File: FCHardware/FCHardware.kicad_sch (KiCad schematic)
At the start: 23 parts, among them J1 XT60Male, J2 Conn_01x02, J3 Conn_01x02, J4 Conn_01x02, J5 Conn_01x02, U1 TPS62125DSG, U2 DRV8833PWP, U3 DRV8833PWP, U5 MPU-6050

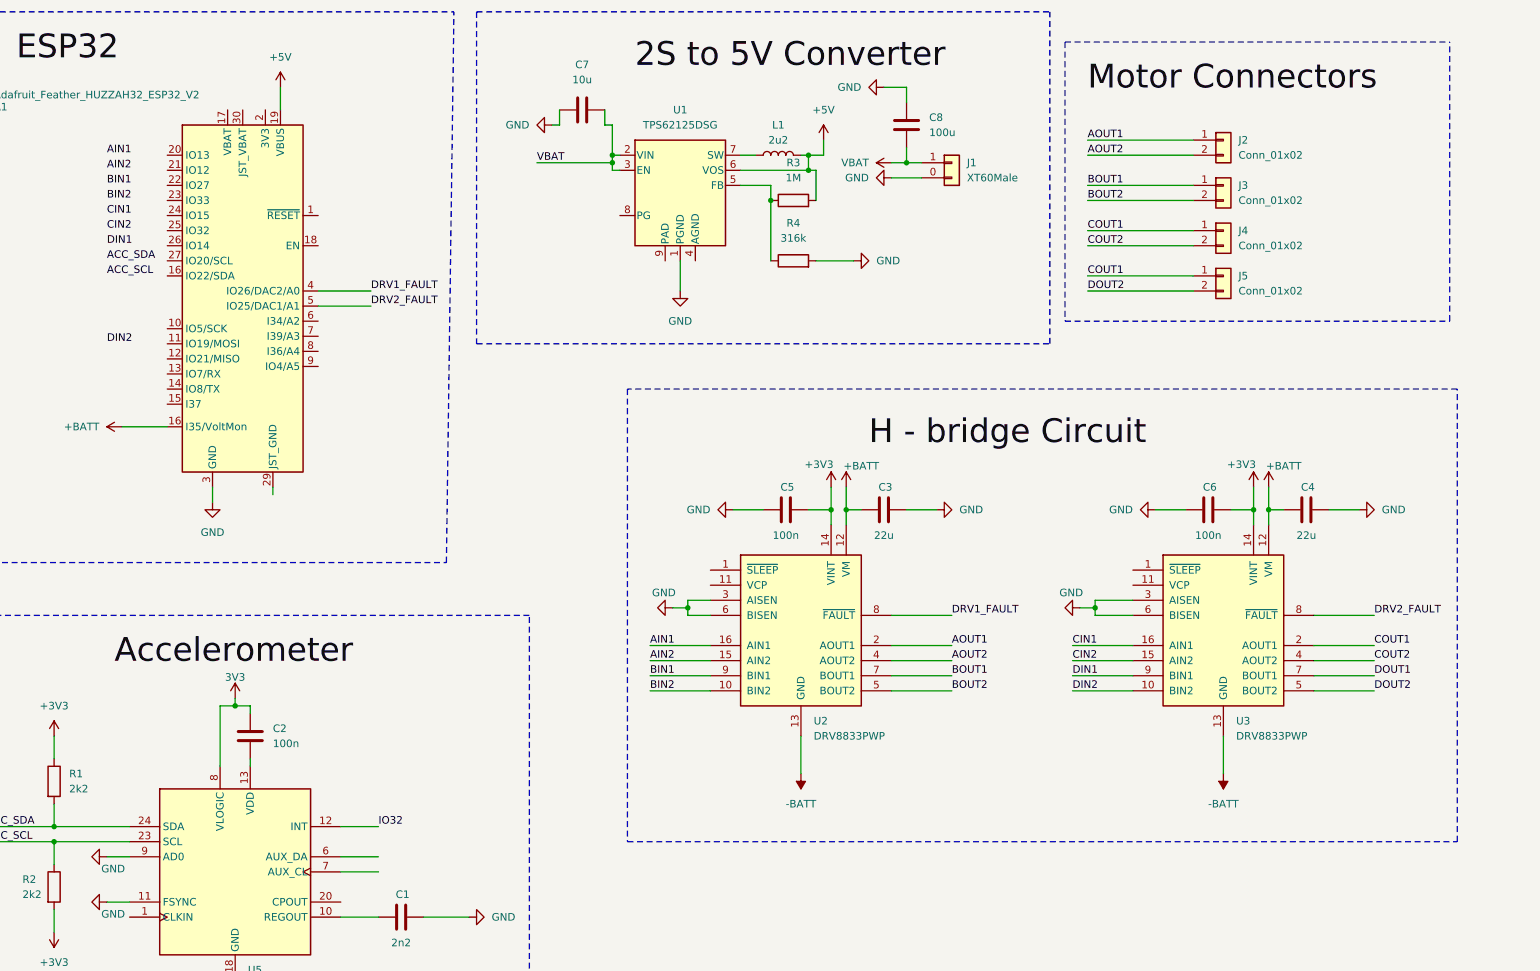
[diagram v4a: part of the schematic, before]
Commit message: Switched from TPS62125 to TPS629203
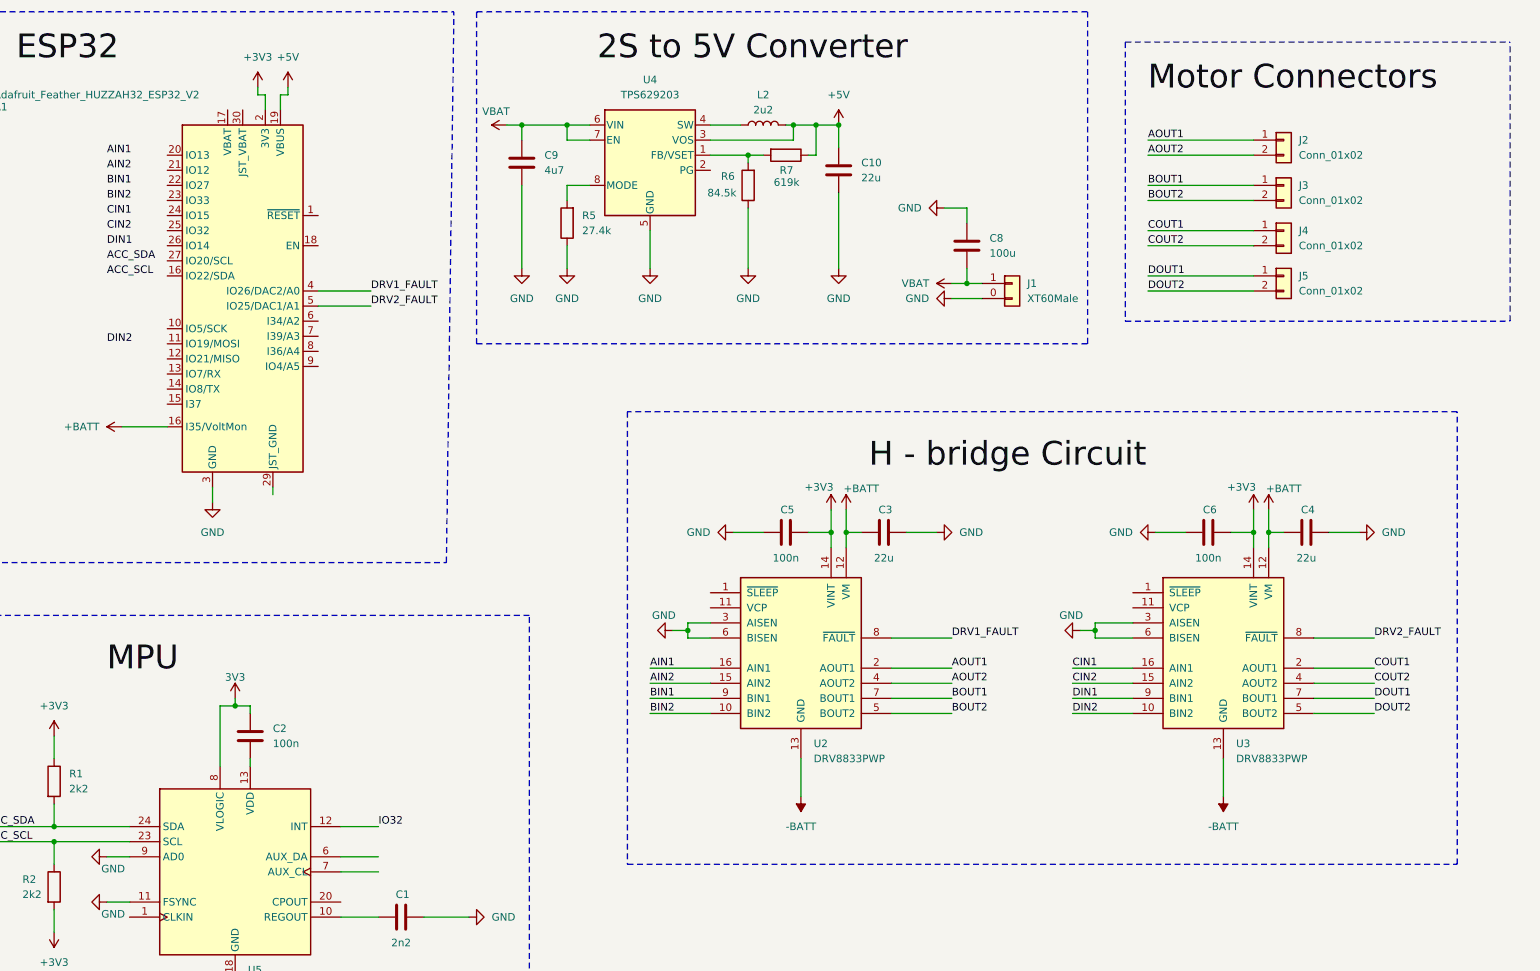
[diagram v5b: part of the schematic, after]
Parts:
- removed C7: 10u, symbol Device:C
- removed L1: 2u2, symbol Device:L
- removed R3: 1M, symbol Device:R
- removed R4: 316k, symbol Device:R
- removed U1: TPS62125DSG, Package_SON:WSON-8-1EP_2x2mm_P0.5mm_EP0.9x1.6mm_ThermalVias, symbol Regulator_Switching:TPS62125DSG
- added C10: 22u, symbol Device:C
- added C9: 4u7, symbol Device:C
- added L2: 2u2, symbol Device:L
- added R5: 27.4k, symbol Device:R
- added R6: 84.5k, symbol Device:R
- added R7: 619k, symbol Device:R
- added U4: TPS629203, Package_SON:WSON-8-1EP_2x2mm_P0.5mm_EP0.9x1.6mm_ThermalVias, symbol CustomSymbols:TPS629203
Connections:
- net +3V3: now also A1.2 (3V3)
- net +5V: now also C10.1, L2.2, R7.1, U4.3 (VOS)
- net COUT1: no longer J5.1 (Pin_1)
- net DOUT1: now also J5.1 (Pin_1)
- net GND: now also C10.2, C9.2, R5.1, R6.1, U4.5 (GND)
- net VBAT: now also C9.1, U4.6 (VIN), U4.7 (EN)
- new net: R6.2, R7.2, U4.1 (FB/VSET)
- new net: L2.1, U4.4 (SW)
- new net: R5.2, U4.8 (MODE)
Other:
- moved on the sheet: C3, C4, C5, C6, C8, J1, J2, J3, J4, J5, U2, U3

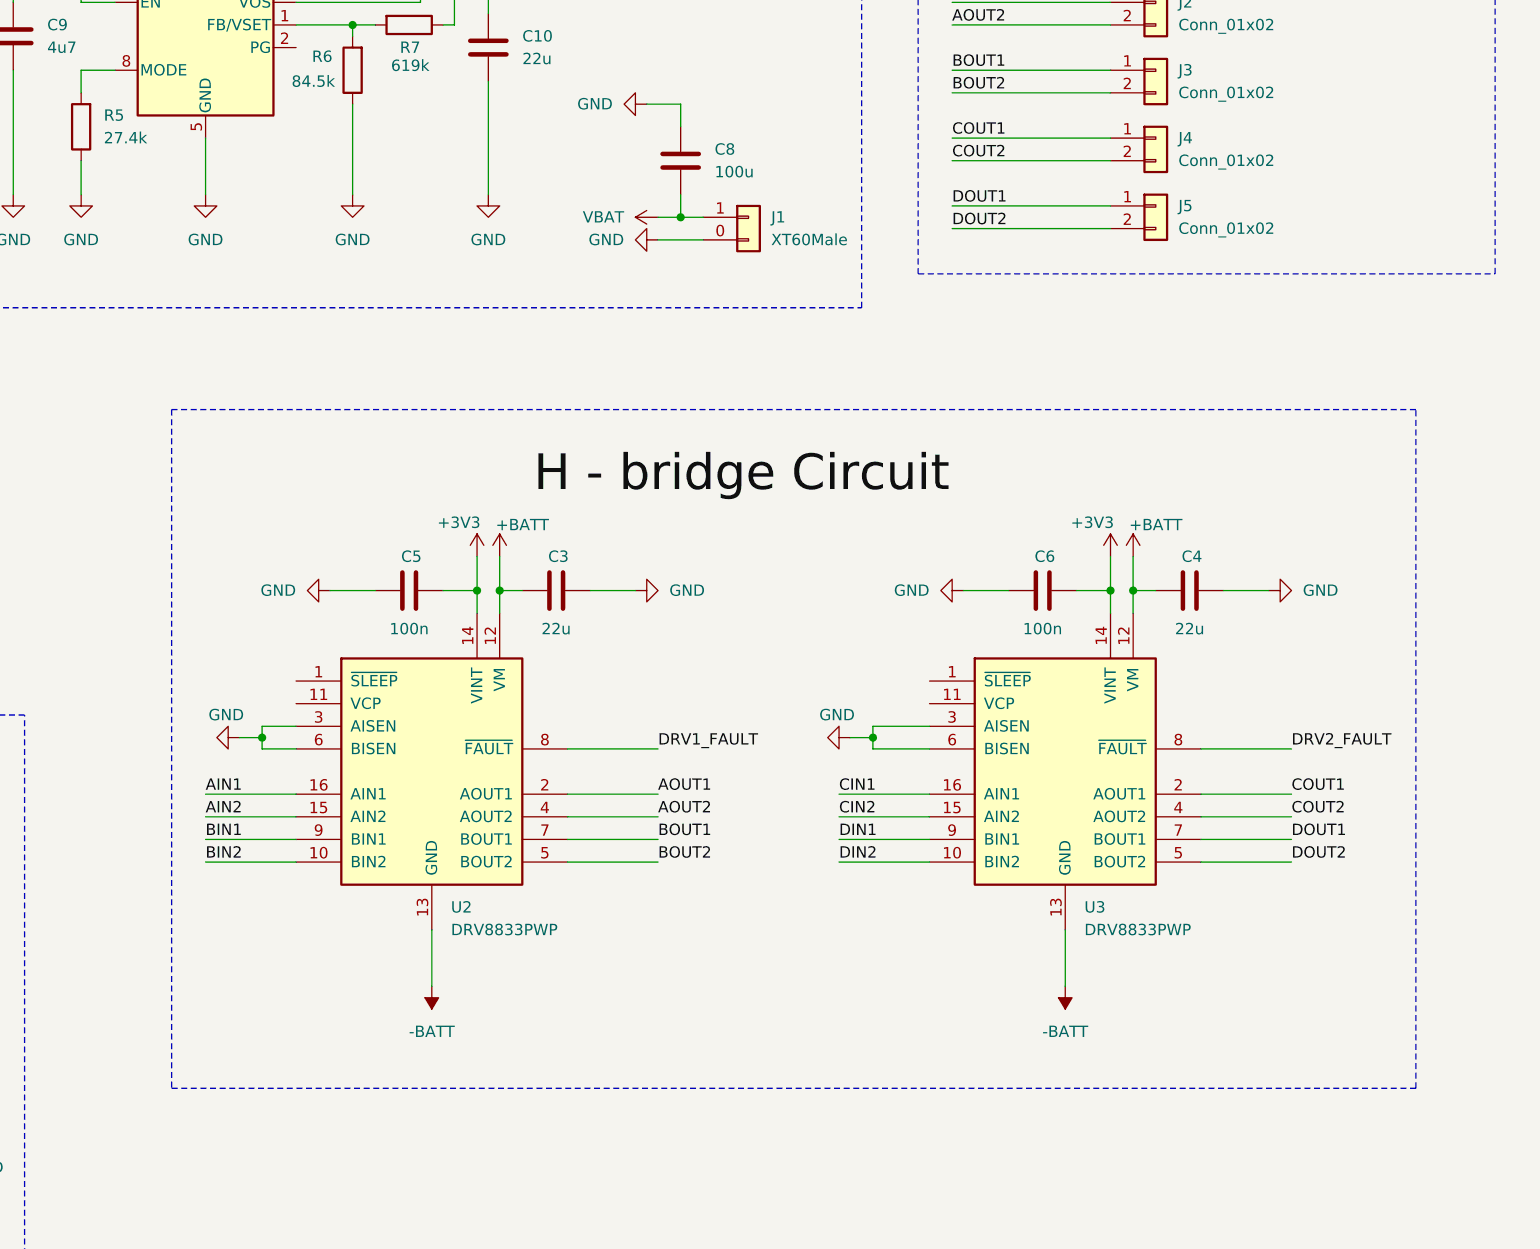
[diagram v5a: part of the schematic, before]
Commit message: Added Xrotor 65A as ESC instead of H-bridges
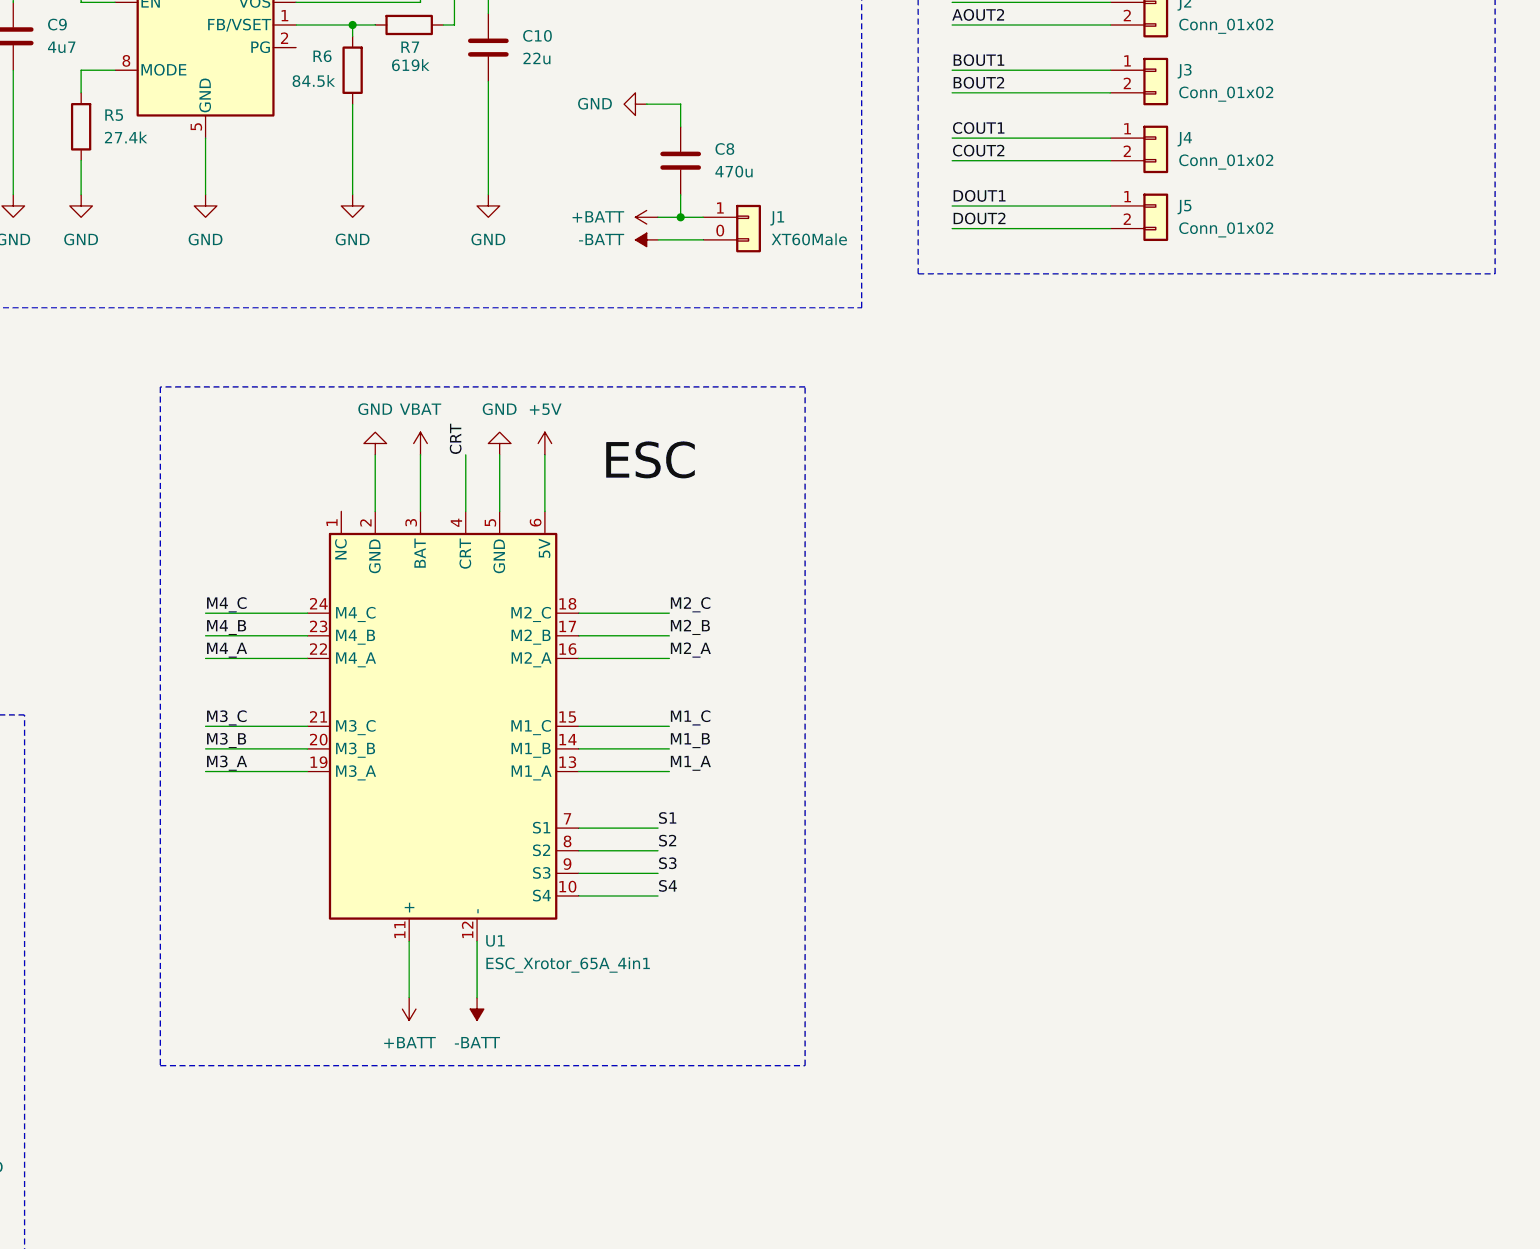
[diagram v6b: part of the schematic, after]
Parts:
- removed C3, C4: 22u, symbol Device:C
- removed C5, C6: 100n, symbol Device:C
- removed U2, U3: DRV8833PWP, Package_SO:HTSSOP-16-1EP_4.4x5mm_P0.65mm_EP3x3mm, symbol Driver_Motor:DRV8833PWP
- added U1: ESC_Xrotor_65A_4in1, -, symbol CustomSymbols:ESC_Xrotor_65A_4in1
- C8: value 100u -> 470u
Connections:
- net +5V: now also U1.6 (5V)
- net +BATT: now also C8.2, J1.1 (+), U1.11 (+)
- net -BATT: now also J1.0 (-), U1.12 (-)
- net GND: now also U1.2 (GND), U1.5 (GND); no longer J1.0 (-)
- net VBAT: now also U1.3 (BAT); no longer C8.2, J1.1 (+)
- new net CRT: U1.4 (CRT)
- new net M1_A: U1.13 (M1_A)
- new net M1_B: U1.14 (M1_B)
- new net M1_C: U1.15 (M1_C)
- new net M2_A: U1.16 (M2_A)
- new net M2_B: U1.17 (M2_B)
- new net M2_C: U1.18 (M2_C)
- new net M3_A: U1.19 (M3_A)
- new net M3_B: U1.20 (M3_B)
- new net M3_C: U1.21 (M3_C)
- new net M4_A: U1.22 (M4_A)
- new net M4_B: U1.23 (M4_B)
- new net M4_C: U1.24 (M4_C)
- new net S1: U1.7 (S1)
- new net S2: U1.8 (S2)
- new net S3: U1.9 (S3)
- new net S4: U1.10 (S4)

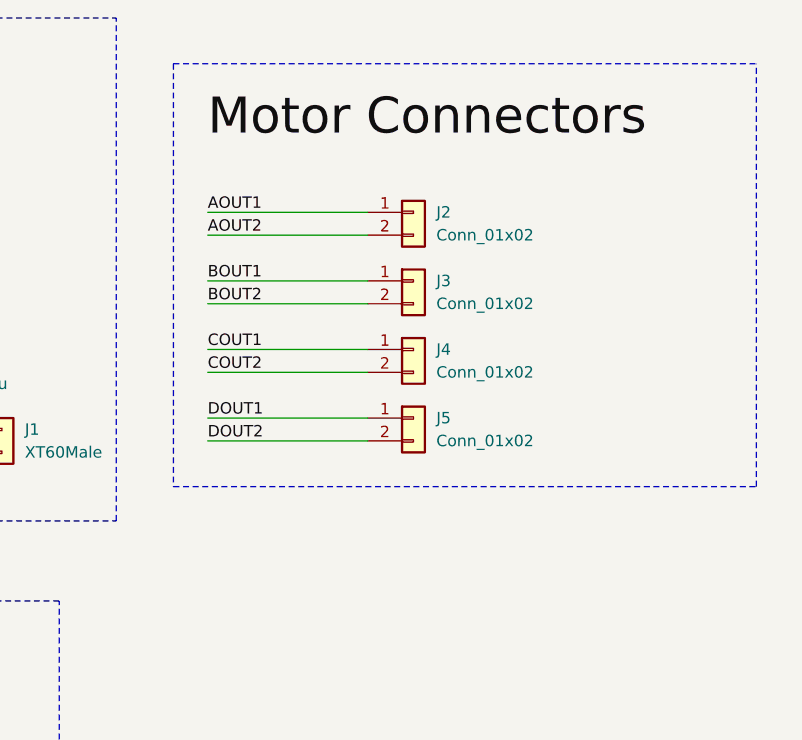
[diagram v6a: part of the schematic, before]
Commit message: Chaged connectors for brushless motors
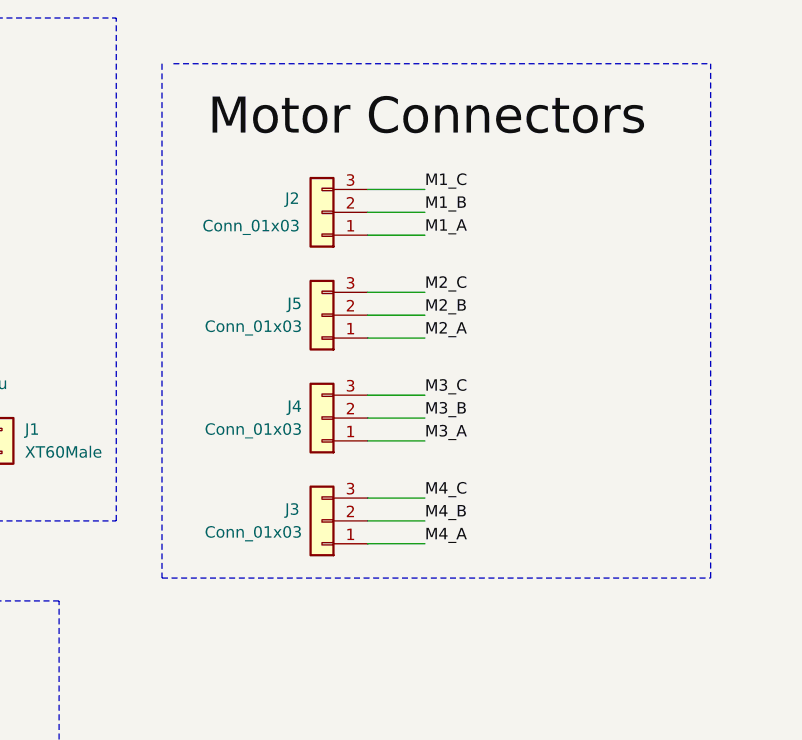
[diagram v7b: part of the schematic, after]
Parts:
- J2, J3, J4, J5: value Conn_01x02 -> Conn_01x03; symbol Connector_Generic:Conn_01x02 -> Connector_Generic:Conn_01x03
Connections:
- net AOUT1 is gone; now on net M1_A: J2.1 (Pin_1)
- net AOUT2 is gone; now on net M1_B: J2.2 (Pin_2)
- net BOUT1 is gone; now on net M4_A: J3.1 (Pin_1)
- net BOUT2 is gone; now on net M4_B: J3.2 (Pin_2)
- net COUT1 is gone; now on net M3_A: J4.1 (Pin_1)
- net COUT2 is gone; now on net M3_B: J4.2 (Pin_2)
- net DOUT1 is gone; now on net M2_A: J5.1 (Pin_1)
- net DOUT2 is gone; now on net M2_B: J5.2 (Pin_2)
- net M1_C: now also J2.3 (Pin_3)
- net M2_C: now also J5.3 (Pin_3)
- net M3_C: now also J4.3 (Pin_3)
- net M4_C: now also J3.3 (Pin_3)
